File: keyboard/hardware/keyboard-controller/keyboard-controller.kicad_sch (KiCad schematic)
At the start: 21 parts, among them J1 Debug_Pins, SW1 RESET, SW2 MODE_SEL, U1 Pico, U2 MCP4921

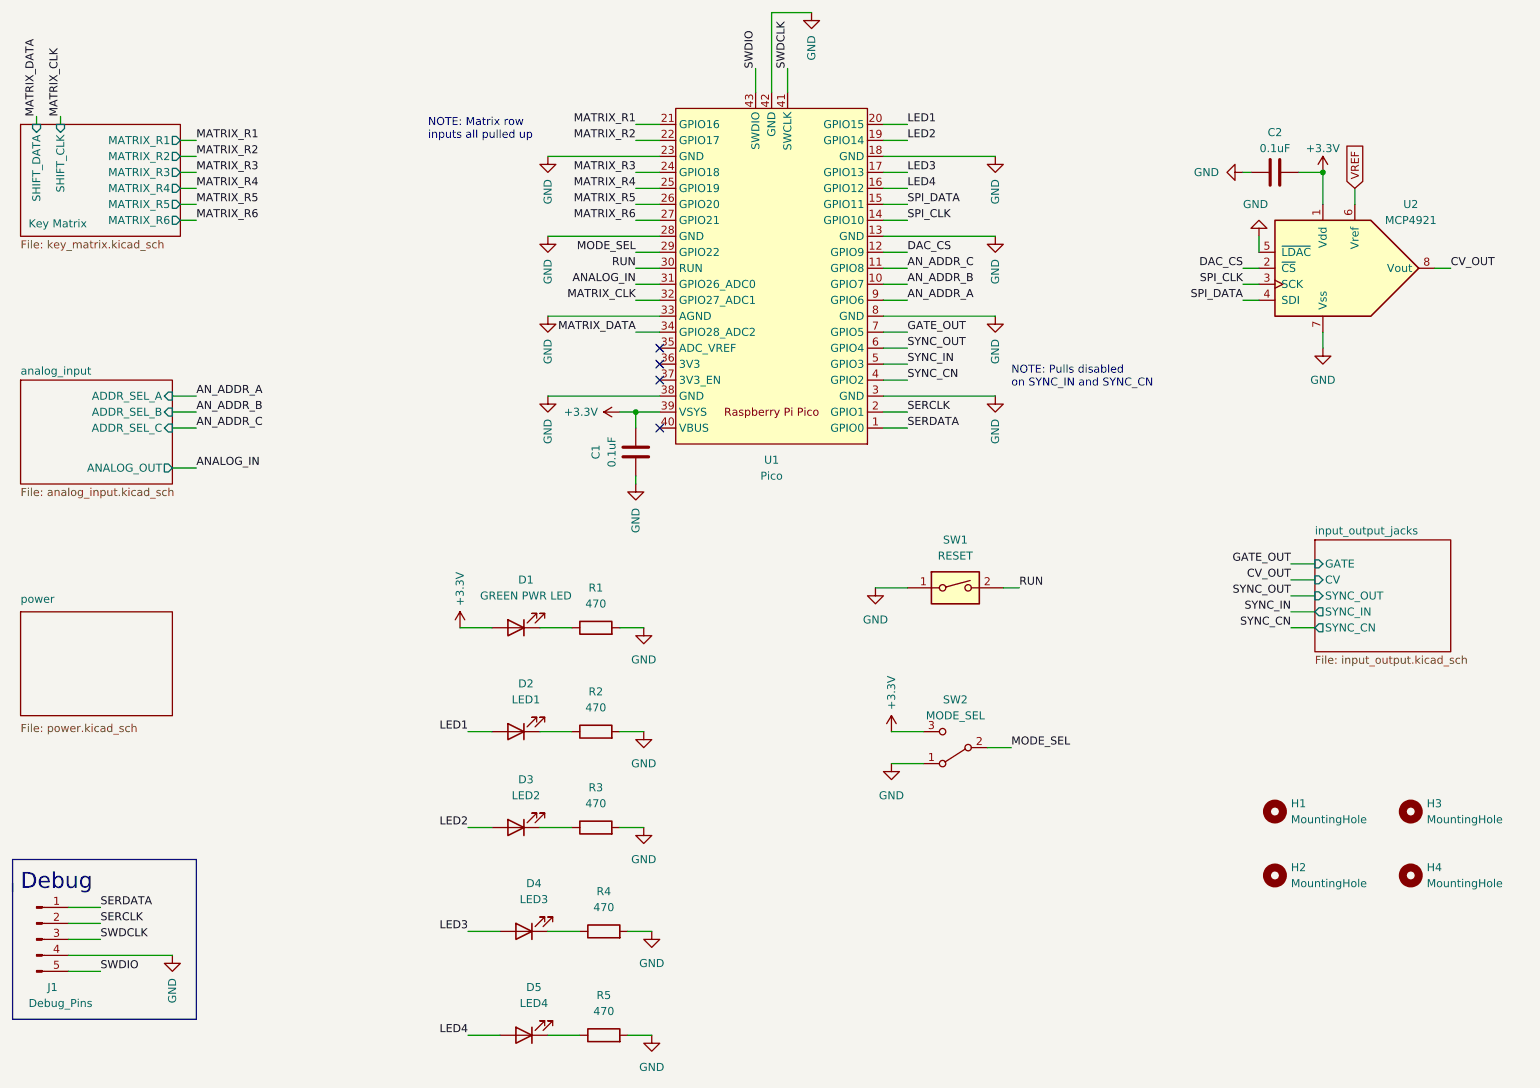
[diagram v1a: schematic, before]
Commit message: Simplified keyboard for rev1
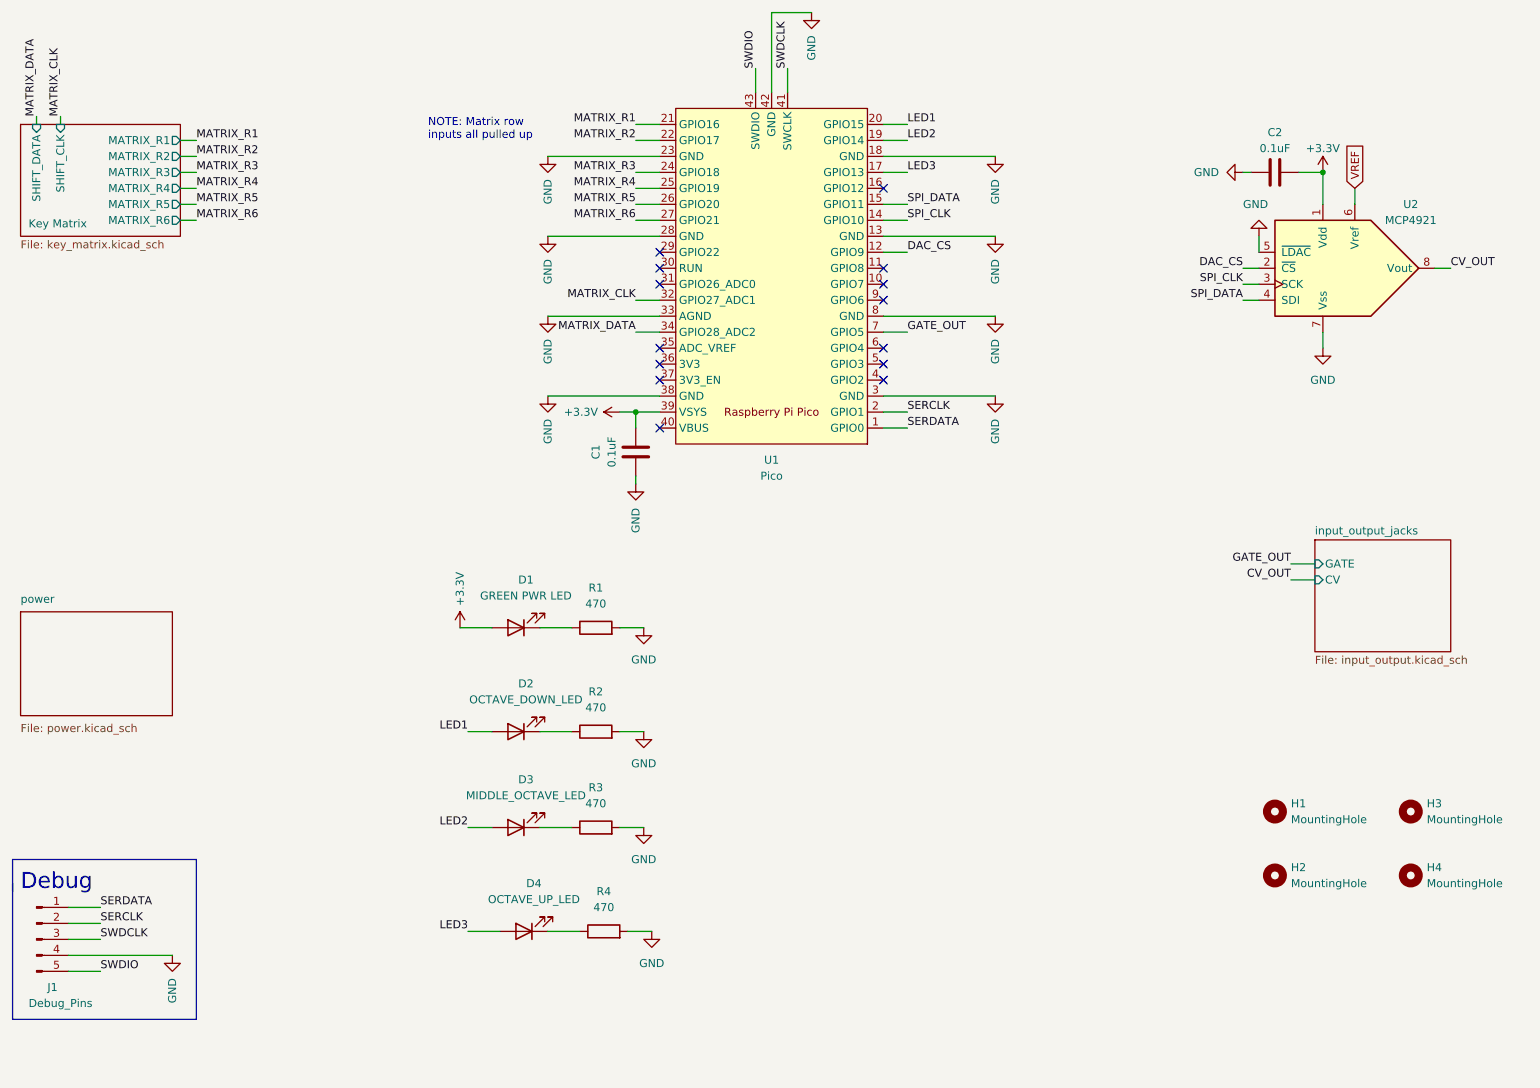
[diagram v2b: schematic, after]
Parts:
- removed D5: LED4, LED_THT:LED_D5.0mm, symbol Device:LED
- removed R5: 470, Royal_Ohm_Resistors:R_Axial_DIN0207_L6.8mm_D2.5mm_P10.16mm_Horizontal, symbol Device:R
- removed SW1: RESET, Button_Switch_THT:SW_PUSH_6mm, symbol Switch:SW_DIP_x01
- removed SW2: MODE_SEL, Wealth_Metal_Switches:Slide_Switch_SPDT_SS12F44G5, symbol Switch:SW_SPDT
- D2: value LED1 -> OCTAVE_DOWN_LED
- D3: value LED2 -> MIDDLE_OCTAVE_LED
- D4: value LED3 -> OCTAVE_UP_LED
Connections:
- net ANALOG_IN: no longer names the net of U1.31 (GPIO26_ADC0)
- net AN_ADDR_A: no longer names the net of U1.9 (GPIO6)
- net AN_ADDR_B: no longer names the net of U1.10 (GPIO7)
- net AN_ADDR_C: no longer names the net of U1.11 (GPIO8)
- net LED4: no longer names the net of U1.16 (GPIO12)
- net MODE_SEL: no longer names the net of U1.29 (GPIO22)
- net RUN: no longer names the net of U1.30 (RUN)
- net SYNC_CN: no longer names the net of U1.4 (GPIO2)
- net SYNC_IN: no longer names the net of U1.5 (GPIO3)
- net SYNC_OUT: no longer names the net of U1.6 (GPIO4)
- no-connect marks 4 -> 14
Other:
- removed sheet analog_input
- sheet input_output_jacks ports: added none; removed SYNC_CN, SYNC_IN, SYNC_OUT
- note removed: "NOTE: Pulls disabled on SYNC_IN and SYNC_CN"

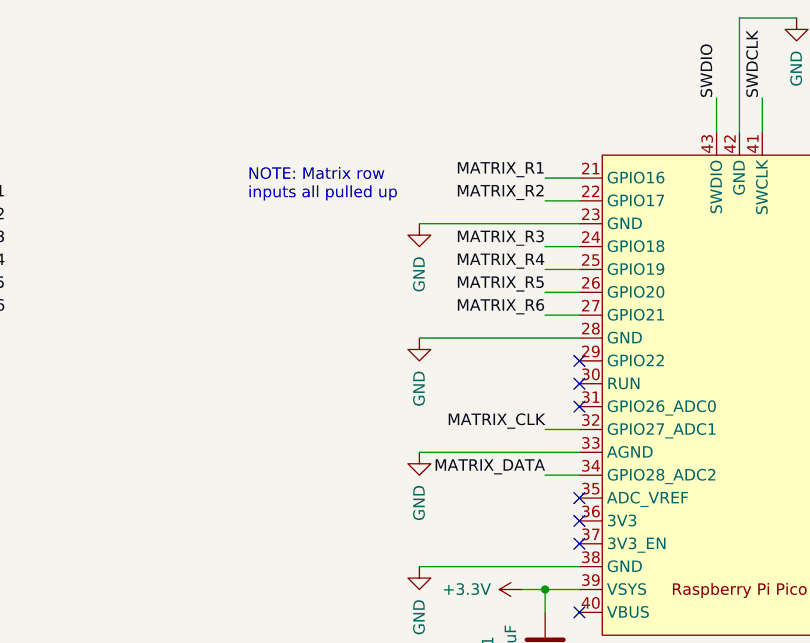
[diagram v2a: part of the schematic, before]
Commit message: Finalized keyboard controller rev1 board
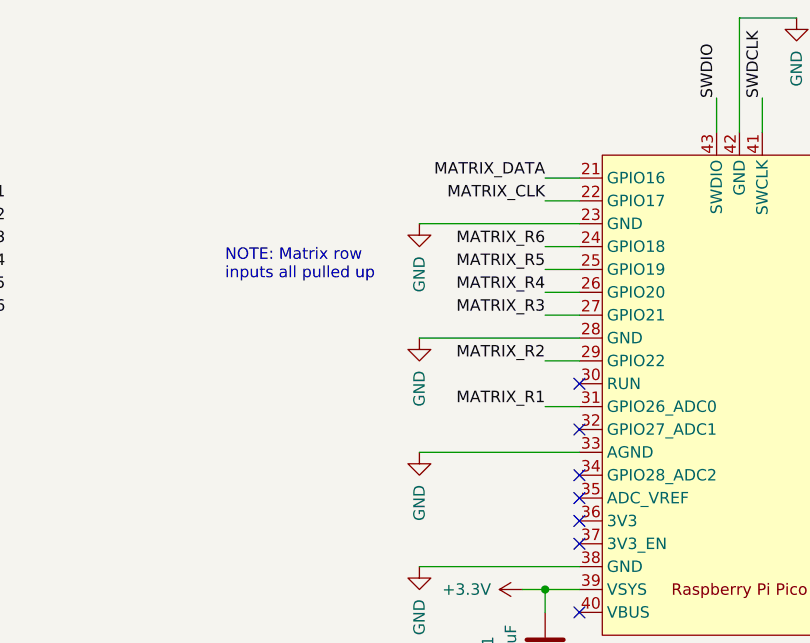
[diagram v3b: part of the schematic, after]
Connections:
- net MATRIX_CLK: now also U1.22 (GPIO17); no longer U1.32 (GPIO27_ADC1)
- net MATRIX_DATA: now also U1.21 (GPIO16); no longer U1.34 (GPIO28_ADC2)
- net MATRIX_R1: now also U1.31 (GPIO26_ADC0); no longer U1.21 (GPIO16)
- net MATRIX_R2: now also U1.29 (GPIO22); no longer U1.22 (GPIO17)
- net MATRIX_R3: now also U1.27 (GPIO21); no longer U1.24 (GPIO18)
- net MATRIX_R4: now also U1.26 (GPIO20); no longer U1.25 (GPIO19)
- net MATRIX_R5: now also U1.25 (GPIO19); no longer U1.26 (GPIO20)
- net MATRIX_R6: now also U1.24 (GPIO18); no longer U1.27 (GPIO21)

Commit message: Fixes to keyboard controller rev1
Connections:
- net GND: no longer U1.13 (GND), U1.18 (GND), U1.23 (GND), U1.28 (GND), U1.3 (GND), U1.8 (GND)
- no-connect marks 14 -> 20
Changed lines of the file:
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@@
   (no_connect (at 170.18 49.53))
   (no_connect (at 134.62 87.63))
+  (no_connect (at 170.18 82.55))
+  (no_connect (at 170.18 69.85))
+  (no_connect (at 170.18 57.15))
+  (no_connect (at 170.18 44.45))
+  (no_connect (at 134.62 57.15))
+  (no_connect (at 134.62 44.45))
   (no_connect (at 134.62 62.23))
   (polyline (pts (xy 31.75 156.21) (xy 31.75 161.29))
@@
     (stroke (width 0) (type default) (color 0 0 0 0))
   )
-  (wire (pts (xy 116.84 44.45) (xy 134.62 44.45))
-    (stroke (width 0) (type default) (color 0 0 0 0))
-  )
   (wire (pts (xy 149.86 30.48) (xy 149.86 34.29))
     (stroke (width 0) (type default) (color 0 0 0 0))
@@
     (stroke (width 0) (type default) (color 0 0 0 0))
   )
-  (wire (pts (xy 187.96 44.45) (xy 170.18 44.45))
-    (stroke (width 0) (type default) (color 0 0 0 0))
-  )
   (wire (pts (xy 170.18 72.39) (xy 173.99 72.39))
     (stroke (width 0) (type default) (color 0 0 0 0))
@@
     (stroke (width 0) (type default) (color 0 0 0 0))
   )
-  (wire (pts (xy 187.96 69.85) (xy 170.18 69.85))
-    (stroke (width 0) (type default) (color 0 0 0 0))
-  )
   (wire (pts (xy 227.33 46.99) (xy 228.6 46.99))
     (stroke (width 0) (type default) (color 0 0 0 0))
@@
     (stroke (width 0) (type default) (color 0 0 0 0))
   )
-  (wire (pts (xy 170.18 82.55) (xy 187.96 82.55))
-    (stroke (width 0) (type default) (color 0 0 0 0))
-  )
-  (wire (pts (xy 187.96 57.15) (xy 170.18 57.15))
-    (stroke (width 0) (type default) (color 0 0 0 0))
-  )
   (wire (pts (xy 152.4 34.29) (xy 152.4 21.59))
     (stroke (width 0) (type default) (color 0 0 0 0))
@@
   )
   (wire (pts (xy 40.64 163.83) (xy 45.72 163.83))
-    (stroke (width 0) (type default) (color 0 0 0 0))
-  )
-  (wire (pts (xy 116.84 57.15) (xy 134.62 57.15))
     (stroke (width 0) (type default) (color 0 0 0 0))
   )
@@
     (pin "1")
   )
-  (symbol (lib_id "power:GND") (at 116.84 57.15 0) (unit 1)
-    (in_bom yes) (on_board yes)
-    (property "Reference" "#PWR04" (id 0) (at 116.84 63.5 0)
-      (effects (font (size 1.27 1.27)) hide)
-    )
-    (property "Value" "GND" (id 1) (at 116.84 64.77 90)
-      (effects (font (size 1.27 1.27)) (justify left))
-    )
-    (property "Footprint" "" (id 2) (at 116.84 57.15 0)
-      (effects (font (size 1.27 1.27)) hide)
-    )
-    (property "Datasheet" "" (id 3) (at 116.84 57.15 0)
-      (effects (font (size 1.27 1.27)) hide)
-    )
-    (pin "1")
-  )
   (symbol (lib_id "power:GND") (at 240.03 74.93 0) (unit 1)
     (in_bom yes) (on_board yes) (fields_autoplaced)
@@
     )
     (property "Datasheet" "" (id 3) (at 128.27 85.09 0)
-      (effects (font (size 1.27 1.27)) hide)
-    )
-    (pin "1")
-  )
-  (symbol (lib_id "power:GND") (at 187.96 69.85 0) (mirror y) (unit 1)
-    (in_bom yes) (on_board yes)
-    (property "Reference" "#PWR020" (id 0) (at 187.96 76.2 0)
-      (effects (font (size 1.27 1.27)) hide)
-    )
-    (property "Value" "GND" (id 1) (at 187.96 77.47 90)
-      (effects (font (size 1.27 1.27)) (justify left))
-    )
-    (property "Footprint" "" (id 2) (at 187.96 69.85 0)
-      (effects (font (size 1.27 1.27)) hide)
-    )
-    (property "Datasheet" "" (id 3) (at 187.96 69.85 0)
       (effects (font (size 1.27 1.27)) hide)
     )
@@
     (pin "2")
   )
-  (symbol (lib_id "power:GND") (at 187.96 44.45 0) (mirror y) (unit 1)
-    (in_bom yes) (on_board yes)
-    (property "Reference" "#PWR018" (id 0) (at 187.96 50.8 0)
-      (effects (font (size 1.27 1.27)) hide)
-    )
-    (property "Value" "GND" (id 1) (at 187.96 52.07 90)
-      (effects (font (size 1.27 1.27)) (justify left))
-    )
-    (property "Footprint" "" (id 2) (at 187.96 44.45 0)
-      (effects (font (size 1.27 1.27)) hide)
-    )
-    (property "Datasheet" "" (id 3) (at 187.96 44.45 0)
-      (effects (font (size 1.27 1.27)) hide)
-    )
-    (pin "1")
-  )
   (symbol (lib_id "Device:LED") (at 113.03 167.64 180) (unit 1)
     (in_bom yes) (on_board yes)
@@
     )
   )
-  (symbol (lib_id "power:GND") (at 187.96 57.15 0) (mirror y) (unit 1)
-    (in_bom yes) (on_board yes)
-    (property "Reference" "#PWR019" (id 0) (at 187.96 63.5 0)
-      (effects (font (size 1.27 1.27)) hide)
-    )
-    (property "Value" "GND" (id 1) (at 187.96 64.77 90)
-      (effects (font (size 1.27 1.27)) (justify left))
-    )
-    (property "Footprint" "" (id 2) (at 187.96 57.15 0)
-      (effects (font (size 1.27 1.27)) hide)
-    )
-    (property "Datasheet" "" (id 3) (at 187.96 57.15 0)
-      (effects (font (size 1.27 1.27)) hide)
-    )
-    (pin "1")
-  )
   (symbol (lib_id "Device:C") (at 130.81 91.44 180) (unit 1)
     (in_bom yes) (on_board yes)
@@
     (pin "1")
     (pin "2")
-  )
-  (symbol (lib_id "power:GND") (at 116.84 44.45 0) (unit 1)
-    (in_bom yes) (on_board yes)
-    (property "Reference" "#PWR03" (id 0) (at 116.84 50.8 0)
-      (effects (font (size 1.27 1.27)) hide)
-    )
-    (property "Value" "GND" (id 1) (at 116.84 52.07 90)
-      (effects (font (size 1.27 1.27)) (justify left))
-    )
-    (property "Footprint" "" (id 2) (at 116.84 44.45 0)
-      (effects (font (size 1.27 1.27)) hide)
-    )
-    (property "Datasheet" "" (id 3) (at 116.84 44.45 0)
-      (effects (font (size 1.27 1.27)) hide)
-    )
-    (pin "1")
   )
   (symbol (lib_id "Device:LED") (at 111.76 135.89 180) (unit 1)
@@
     (pin "1")
   )
-  (symbol (lib_id "power:GND") (at 187.96 82.55 0) (mirror y) (unit 1)
-    (in_bom yes) (on_board yes)
-    (property "Reference" "#PWR021" (id 0) (at 187.96 88.9 0)
-      (effects (font (size 1.27 1.27)) hide)
-    )
-    (property "Value" "GND" (id 1) (at 187.96 90.17 90)
-      (effects (font (size 1.27 1.27)) (justify left))
-    )
-    (property "Footprint" "" (id 2) (at 187.96 82.55 0)
-      (effects (font (size 1.27 1.27)) hide)
-    )
-    (property "Datasheet" "" (id 3) (at 187.96 82.55 0)
-      (effects (font (size 1.27 1.27)) hide)
-    )
-    (pin "1")
-  )
   (symbol (lib_id "power:GND") (at 116.84 69.85 0) (unit 1)
     (in_bom yes) (on_board yes)
@@
       (reference "#PWR02") (unit 1) (value "+3.3V") (footprint "")
     )
-    (path "/d88145b4-2add-4c5d-9a98-fddf1d0075d2"
-      (reference "#PWR03") (unit 1) (value "GND") (footprint "")
-    )
-    (path "/1e362628-defa-47c2-8e50-53580a9b604b"
-      (reference "#PWR04") (unit 1) (value "GND") (footprint "")
-    )
     (path "/f7eedf75-4d8e-4db5-a979-879f661d7288"
       (reference "#PWR05") (unit 1) (value "GND") (footprint "")
@@
       (reference "#PWR014") (unit 1) (value "GND") (footprint "")
     )
-    (path "/76f2227d-64f6-4788-b1e5-026d957818a2"
-      (reference "#PWR018") (unit 1) (value "GND") (footprint "")
-    )
-    (path "/b32baf8d-6550-4238-9c71-ca9f9a9ac4fa"
-      (reference "#PWR019") (unit 1) (value "GND") (footprint "")
-    )
-    (path "/3bdf0db5-95fa-40cc-b340-ff31b9761a6f"
-      (reference "#PWR020") (unit 1) (value "GND") (footprint "")
-    )
-    (path "/f78c359c-eb13-4e17-9480-28a818c48519"
-      (reference "#PWR021") (unit 1) (value "GND") (footprint "")
-    )
     (path "/cff19a40-3182-44ce-8fc2-e0cd9e8f8ffb"
       (reference "#PWR022") (unit 1) (value "GND") (footprint "")
@@
       (reference "#PWR059") (unit 1) (value "GND") (footprint "")
     )
-    (path "/db9d31eb-90c6-4f42-b97b-d41061869d3f/698a5a92-9909-457d-bd27-95c21d74ec53"
-      (reference "#PWR0101") (unit 1) (value "GND") (footprint "")
-    )
     (path "/c0e681eb-c54c-4cf9-ad72-7f86fd2061ac"
       (reference "C1") (unit 1) (value "0.1uF") (footprint "AEC_Capacitors:C_Disc_D5.0mm_W2.5mm_P3.0mm")
@@
     )
     (path "/db9d31eb-90c6-4f42-b97b-d41061869d3f/2b7a9ebe-7331-48bd-9d79-b8105343e150"
-      (reference "SW3") (unit 1) (value "OCTAVE_UP") (footprint "Button_Switch_THT:SW_PUSH_6mm")
+      (reference "SW3") (unit 1) (value "FUNC") (footprint "Button_Switch_THT:SW_PUSH_6mm")
     )
     (path "/db9d31eb-90c6-4f42-b97b-d41061869d3f/6e018595-390d-4323-9807-30f2419acc34"
-      (reference "SW4") (unit 1) (value "OCTAVE_DOWN") (footprint "Button_Switch_THT:SW_PUSH_6mm")
+      (reference "SW4") (unit 1) (value "OCTAVE_UP") (footprint "Button_Switch_THT:SW_PUSH_6mm")
     )
     (path "/db9d31eb-90c6-4f42-b97b-d41061869d3f/78450e1c-f3c0-405d-917c-77aaef99c6a6"
-      (reference "SW5") (unit 1) (value "FUNC") (footprint "Button_Switch_THT:SW_PUSH_6mm")
+      (reference "SW5") (unit 1) (value "OCTAVE_DOWN") (footprint "Button_Switch_THT:SW_PUSH_6mm")
     )
     (path "/4dab636c-209c-4c09-a308-acd258d99642"

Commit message: Completed keyboard controller rev2
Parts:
- added TP1: CV_PRE, TestPoint:TestPoint_Pad_D1.5mm, symbol Connector:TestPoint
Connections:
- net CV_OUT: now also TP1.1
